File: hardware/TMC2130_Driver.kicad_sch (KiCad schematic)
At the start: 35 parts, among them J1 PCIe_Stepper, J2 Conn_01x04_Male, J3 Screw_Terminal_01x02, U1 TMC2130, U2 24LC02

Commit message: Update 2660 and 2130 driver fab files.
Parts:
- FID1, FID2, FID3, FID4, H1, H2, LOGO1: now left out of the parts list
- U2: LCSC Part # C184154 -> C184154

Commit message: Convert SCH files to latest version. Fix DRC Warnings in PrntrBoard.
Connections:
- net ~CS renamed ~{CS}
- net ~ENABLE renamed ~{ENABLE}
- net ~RESET renamed ~{RESET}
- net ~SLEEP renamed ~{SLEEP}

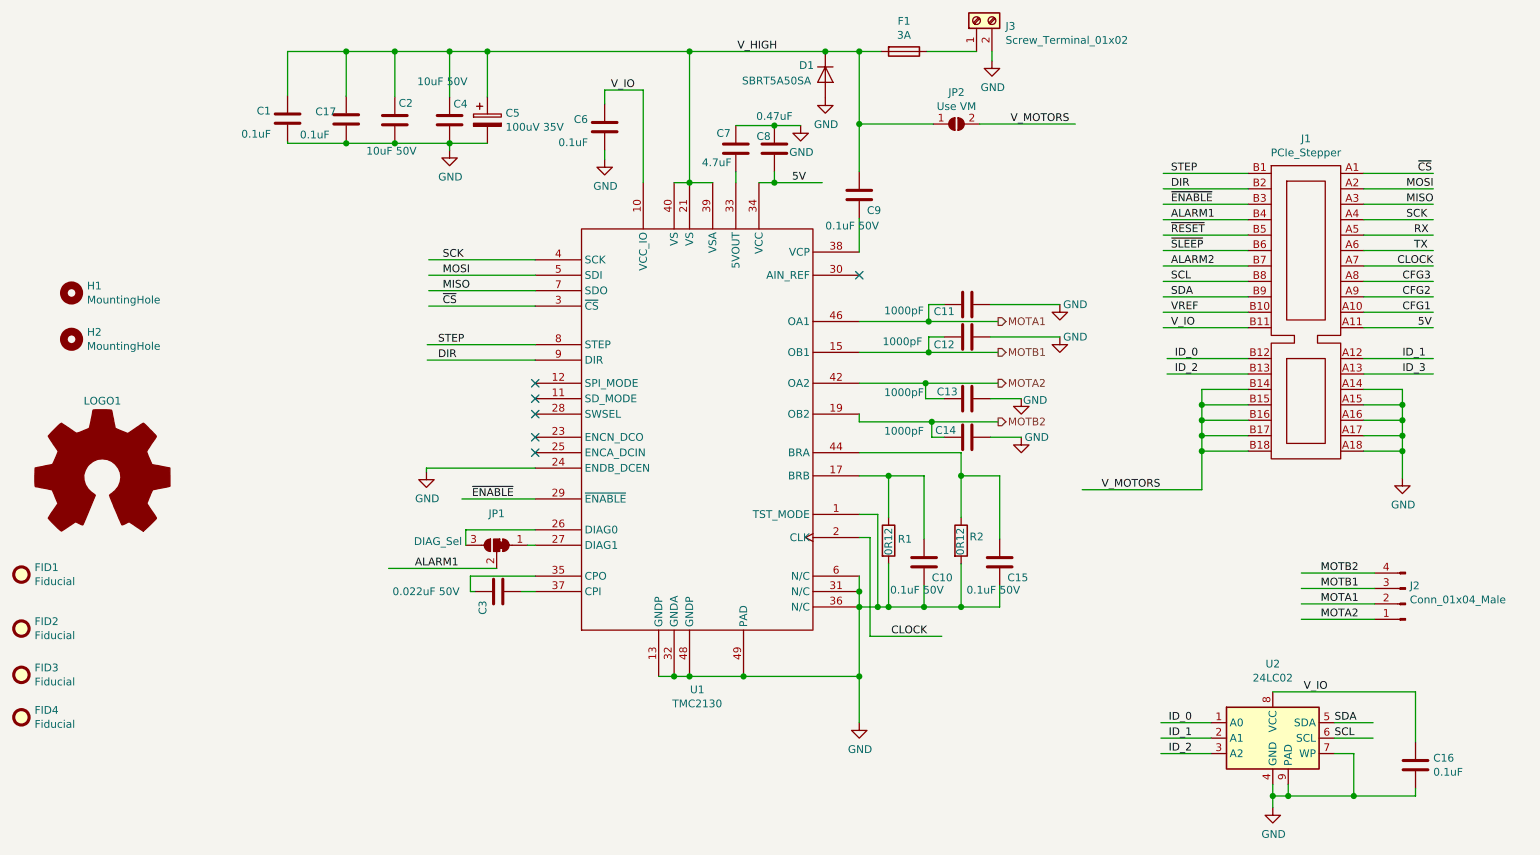
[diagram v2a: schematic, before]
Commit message: Update drivers to respect high motor coltage circuit.
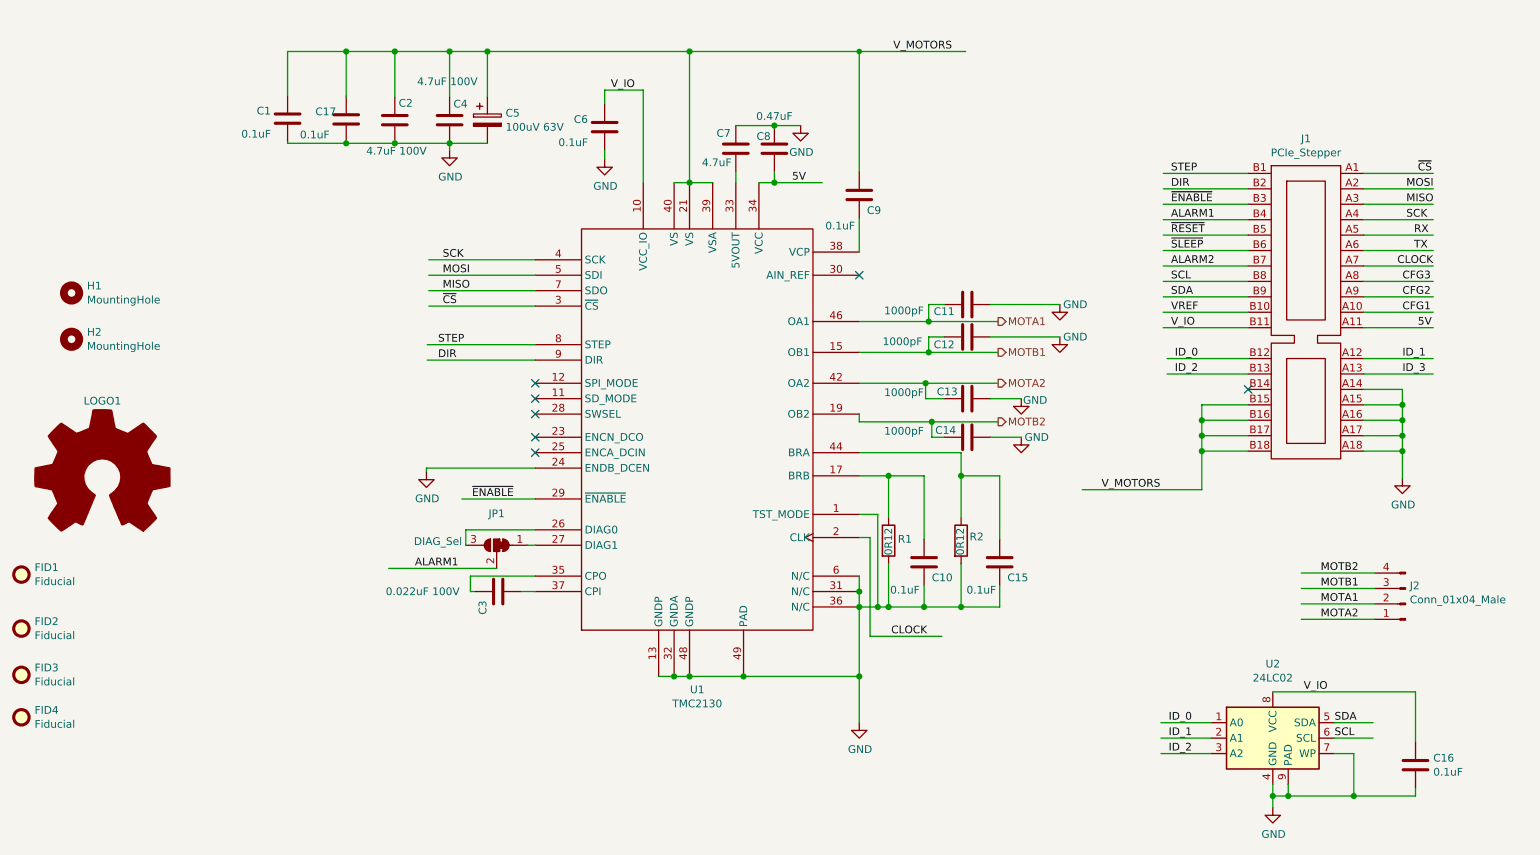
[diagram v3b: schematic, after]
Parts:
- removed D1: SBRT5A50SA, Diode_SMD:D_SMA, symbol Device:D
- removed F1: 3A, Fuse:Fuse_1206_3216Metric, symbol Device:Fuse
- removed J3: Screw_Terminal_01x02, TerminalBlock_Phoenix:TerminalBlock_Phoenix_PT-1,5-2-3.5-H_1x02_P3.50mm_Horizontal, symbol Connector:Screw_Terminal_01x02
- removed JP2: Use VM, Jumper:SolderJumper-2_P1.3mm_Open_TrianglePad1.0x1.5mm, symbol Jumper:SolderJumper_2_Open
- C1, C17: footprint PrntrBoardV2:C_0603_1608Metric -> Capacitor_SMD:C_0805_2012Metric; LCSC Part # C14663 -> C28233; Part # CC0603KRX7R9BB104 -> CL21B104KCFNNNE
- C10, C15: value 0.1uF 50V -> 0.1uF; footprint PrntrBoardV2:C_0402_1005Metric -> Capacitor_SMD:C_0805_2012Metric; LCSC Part # C1525 -> C28233; Part # CL05B104KO5NNNC -> HMK325C7475KN-TE
- C11, C12, C13, C14: LCSC Part # C1588 -> C153291; Part # CL10B102KB8NNNC -> CL10B102KC8NNNC
- C2, C4: value 10uF 50V -> 4.7uF 100V; footprint PrntrBoardV2:C_1206_3216Metric -> Capacitor_SMD:C_1210_3225Metric; LCSC Part # C13585 -> C697607; Part # CL31A106KBHNNNE -> HMK325C7475KN-TE
- C3: value 0.022uF 50V -> 0.022uF 100V; footprint PrntrBoardV2:C_0603_1608Metric -> Capacitor_SMD:C_0805_2012Metric; LCSC Part # C21122 -> C313105; Part # CL10B223KB8NNNC -> CC0603KRX7R0BB223
- C5: value 100uV 35V -> 100uV 63V; footprint Capacitor_SMD:CP_Elec_6.3x7.7 -> Capacitor_SMD:CP_Elec_10x10.5; LCSC Part # C171732 -> C263945; Part # VE-101M1VTR-0607 -> CK1J101MCRG10
- C9: value 0.1uF 50V -> 0.1uF; footprint PrntrBoardV2:C_0402_1005Metric -> Capacitor_SMD:C_0805_2012Metric; LCSC Part # C1525 -> C28233; Part # CL05B104KO5NNNC -> CL21B104KCFNNNE
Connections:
- net V_HIGH is gone; now on net V_MOTORS: C1.1, C17.1, C2.1, C4.1, C5.1, C9.1, U1.21 (VS), U1.39 (VSA), U1.40 (VS)
- net V_MOTORS: no longer J1.B14
- no-connect marks 6 -> 7
